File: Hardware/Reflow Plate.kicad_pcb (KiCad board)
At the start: 2 copper layers, 99.1 x 99.1 mm, 33 parts, among them J2 31-M-12, J3 Conn_02x03_Odd_Even, J4 Conn_02x03_Odd_Even, J5 Conn_02x03_Odd_Even, J6 Conn_02x03_Odd_Even, J7 Conn_01x04_Pin, Q2 Q_NMOS_GDS, U1 HUSB238, U2 AMS1117-3.3, U4 STM32F103RBTx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

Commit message: Add readme, bad power routing, final heater idea. Likely needs new layout.
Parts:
- removed U4: STM32F103RBTx, Package_QFP:LQFP-64_10x10mm_P0.5mm
- added G***: LOGO, footprints:Warning Hot, F.Cu at (139.7, 90.2)
- added J1: Barrel_Jack_MountingPin, footprints:DC Barrel, F.Cu at (97.4, 45.1)
- added MOSFET1: AONR21307, footprints:DFN8_3x3_EP_AOS, F.Cu at (113.5, 39.0)
- added U3: STM32F103CBTx, Package_QFP:LQFP-48_7x7mm_P0.5mm, F.Cu at (153.7, 42.5)
- J2: moved to B.Cu
- moved D2 73.3 mm to (114.2, 42.9)
- moved U1 63.3 mm to (105.4, 38.7)
- moved D1 61.1 mm to (104.1, 45.7), turned to -90 degrees
- moved R3 60.6 mm to (104.4, 36.4), turned to 180 degrees
- moved R2 59.4 mm to (109.9, 39.0), turned to 180 degrees
- moved R1 57.9 mm to (108.2, 37.7), turned to -90 degrees
- moved J2 34.7 mm to (105.4, 38.1), turned to 0 degrees
- moved U2 16.0 mm to (132.1, 25.4)
- moved J7 9.42 mm to (128.3, 38.7)
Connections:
- net GATE renamed Net-(U1-GATE)
- J3 pad 2: unconnected-(J3-Pin_2-Pad2) -> /Heater
- J3 pad 3: /Heater -> unconnected-(J3-Pin_3-Pad3)
- J3 pad 6: unconnected-(J3-Pin_6-Pad6) -> /Heater
- J5 pad 1: +24V -> Net-(J5-Pin_1)
- J5 pad 2: unconnected-(J5-Pin_2-Pad2) -> Net-(J5-Pin_1)
- J5 pad 3: +24V -> unconnected-(J5-Pin_3-Pad3)
- J5 pad 6: unconnected-(J5-Pin_6-Pad6) -> +24V
- Q2 pad 2: Net-(J6-Pin_1) -> Net-(J5-Pin_1)
- R1 pad 2: Net-(Q1-G) -> Net-(MOSFET1-G)
- R2 pad 1: Net-(Q1-G) -> Net-(J2-VBUS-PadA4)
- R2 pad 2: Net-(J2-VBUS-PadA4) -> Net-(MOSFET1-G)
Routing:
- net Net-(J2-VBUS-PadA4): track 0.00 -> 30.8 mm, vias 0 -> 3
- net +24V: track 0.00 -> 11.9 mm
- net UDB_D+: track 0.00 -> 10.8 mm, vias 0 -> 1
- net UDB_D-: track 0.00 -> 10.0 mm, vias 0 -> 1
- net Net-(D1-A): track 0.00 -> 6.86 mm
- net Net-(J2-CC2): track 0.00 -> 5.15 mm, vias 0 -> 1
- net Net-(J2-CC1): track 0.00 -> 4.88 mm, vias 0 -> 1
- net Net-(MOSFET1-G): track 0.00 -> 4.50 mm
- net /Heater: track 2943.6 -> 2941.4 mm
- net Net-(U1-GATE): track 0.00 -> 1.55 mm
- net Net-(U1-VIN): track 0.00 -> 1.31 mm

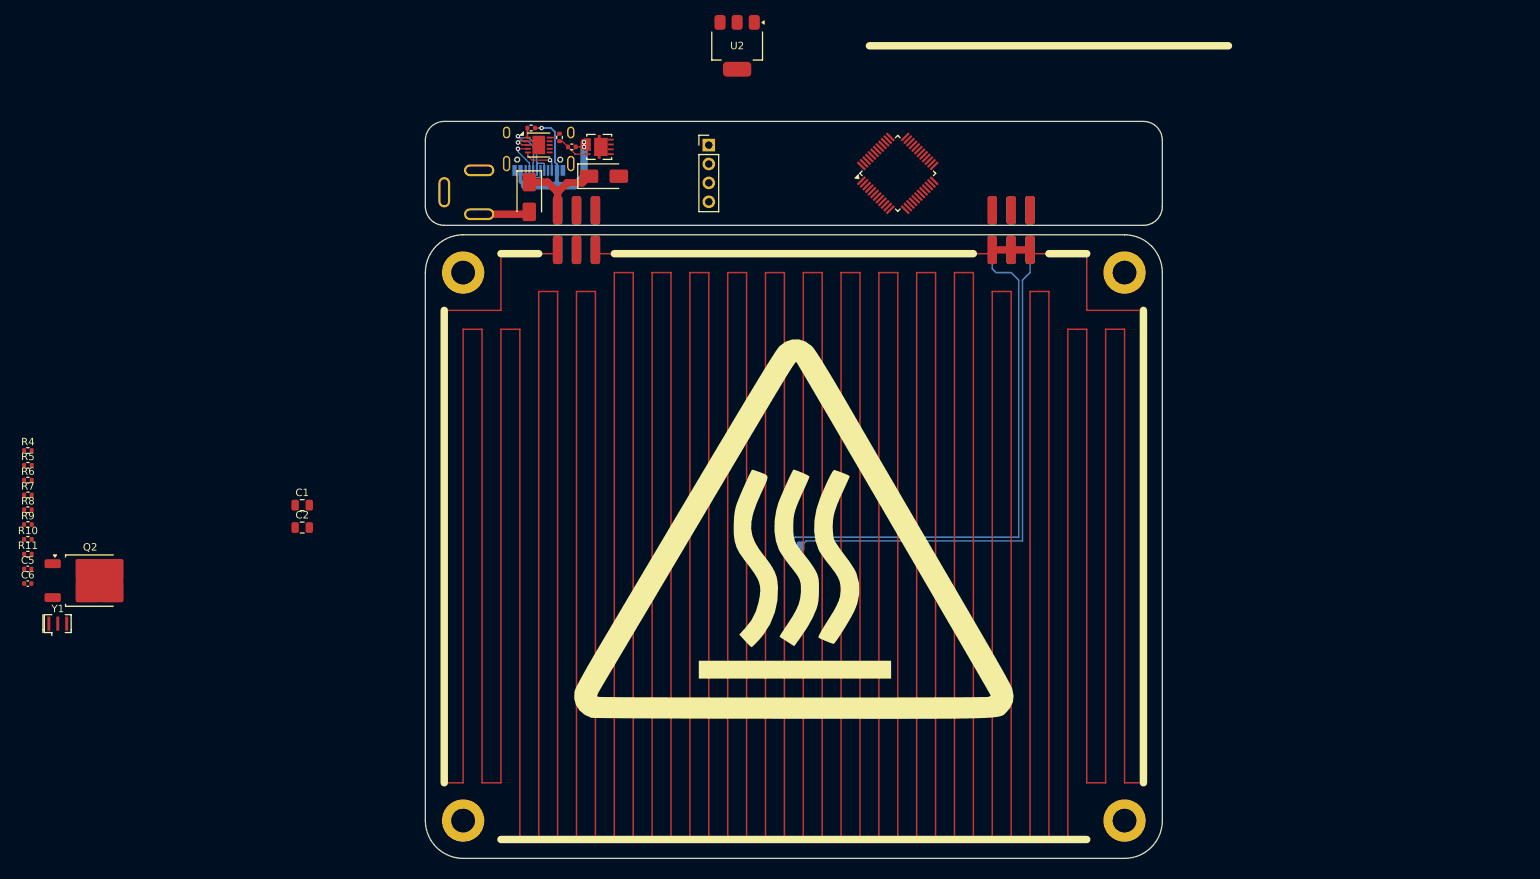
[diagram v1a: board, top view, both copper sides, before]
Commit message: Closer to final placement of power components. Shooting for single sided assembly. Still some scuffed placements. Really packed. Missing likely needed ground planes.
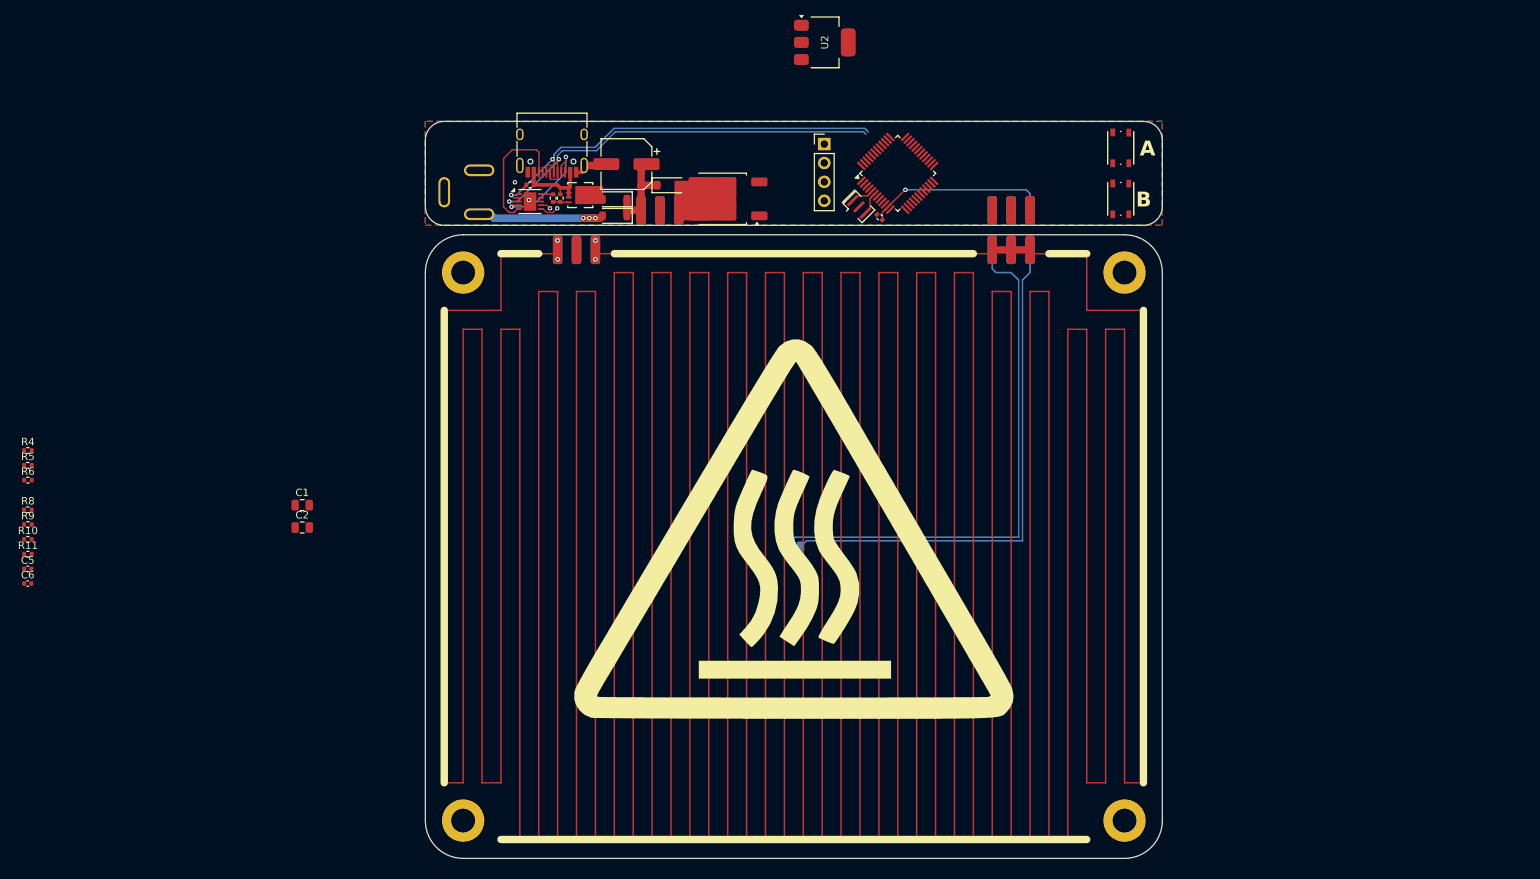
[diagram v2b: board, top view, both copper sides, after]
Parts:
- added C4: 220u, Capacitor_SMD:CP_Elec_6.3x7.7, F.Cu at (117.2, 41.3)
- added D3: D_Zener, Diode_SMD:D_SOD-123, F.Cu at (123.0, 44.1)
- added REF**: SW_Push_1P1T_NO_Vertical_Wuerth_434133025816, Button_Switch_SMD:SW_Push_1P1T_NO_Vertical_Wuerth_434133025816, F.Cu at (183.6, 39.1)
- added REF**: SW_Push_1P1T_NO_Vertical_Wuerth_434133025816, Button_Switch_SMD:SW_Push_1P1T_NO_Vertical_Wuerth_434133025816, F.Cu at (183.6, 46.0)
- D1, D2: footprint Diode_SMD:D_SMA -> Diode_SMD:D_SOD-123
- J2: moved to F.Cu
- moved Y1 121.4 mm to (148.5, 47.0), turned to -45 degrees
- moved R7 120.4 mm to (151.2, 48.4), turned to -45 degrees
- moved Q2 99.2 mm to (130.0, 46.0), turned to 180 degrees
- moved J7 33.2 mm to (161.3, 42.4)
- moved U2 11.8 mm to (143.9, 24.9), turned to 0 degrees
- moved D1 11.8 mm to (115.6, 48.3), turned to 180 degrees
- moved J5 11.2 mm to (121.7, 47.5)
- moved R1 8.20 mm to (107.3, 45.9)
- moved U1 7.68 mm to (104.2, 46.3)
- moved R3 7.65 mm to (104.2, 44.1)
- moved R2 7.06 mm to (108.3, 45.9), turned to -90 degrees
- moved MOSFET1 6.96 mm to (111.0, 45.5)
- moved D2 3.42 mm to (115.6, 46.0), turned to 180 degrees
- moved J2 1.80 mm to (107.2, 38.4), turned to 180 degrees
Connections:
- U3 pad 10: unconnected-(U3-PA0-Pad10) -> WKUP
- U3 pad 13: unconnected-(U3-PA3-Pad13) -> Heater_CTRL
- U3 pad 46: Heater_CTRL -> unconnected-(U3-PB9-Pad46)
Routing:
- net UDB_D-: track 10.0 -> 58.6 mm, vias 1 -> 2
- net UDB_D+: track 10.8 -> 58.1 mm, vias 1 -> 2
- net NTC_Measure: track 0.00 -> 24.6 mm, vias 0 -> 1
- net Net-(J2-VBUS-PadA4): track 30.8 -> 10.8 mm, vias 3 -> 0
- net Net-(J2-CC2): track 5.15 -> 17.2 mm, vias 1 -> 0
- net Net-(D1-A): track 6.86 -> 18.6 mm, vias 0 -> 3
- net Net-(J2-CC1): track 4.88 -> 14.8 mm, vias 1 -> 2
- net GND: track 0.00 -> 4.88 mm, vias 0 -> 2
- net Net-(U3-PD1): track 0.00 -> 3.10 mm
- net Net-(U3-PD0): track 0.00 -> 3.10 mm
- net SDA1: track 0.00 -> 2.62 mm, vias 0 -> 1
- net Net-(MOSFET1-G): track 4.50 -> 2.13 mm
- net SCL1: track 0.00 -> 1.40 mm, vias 0 -> 1
- net +24V: track 11.9 -> 12.8 mm
- net /Heater: vias 0 -> 4
- added copper zone on B.Cu, net GND
- added copper zone on F.Cu, net GND
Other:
- board text added: "A"
- board text added: "B"

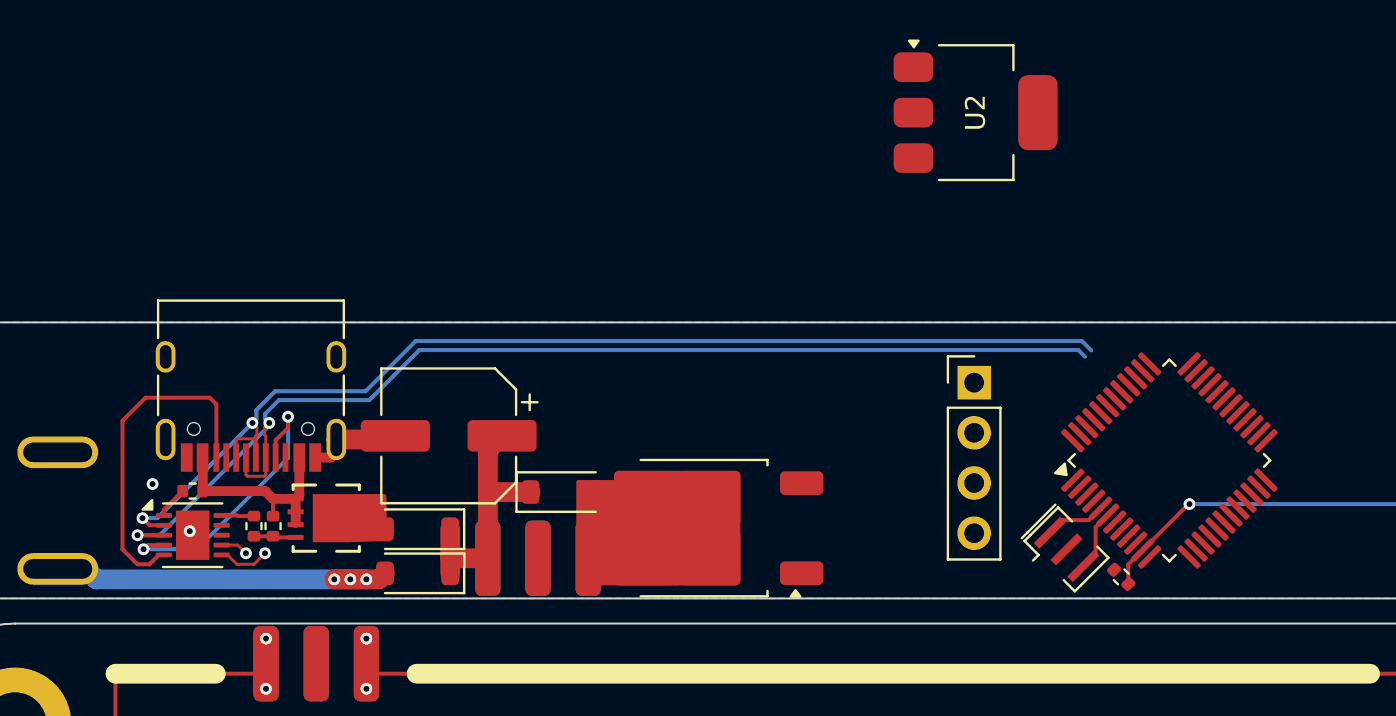
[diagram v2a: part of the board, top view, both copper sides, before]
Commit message: Final power layout. Changing LDO to SOT-23-5
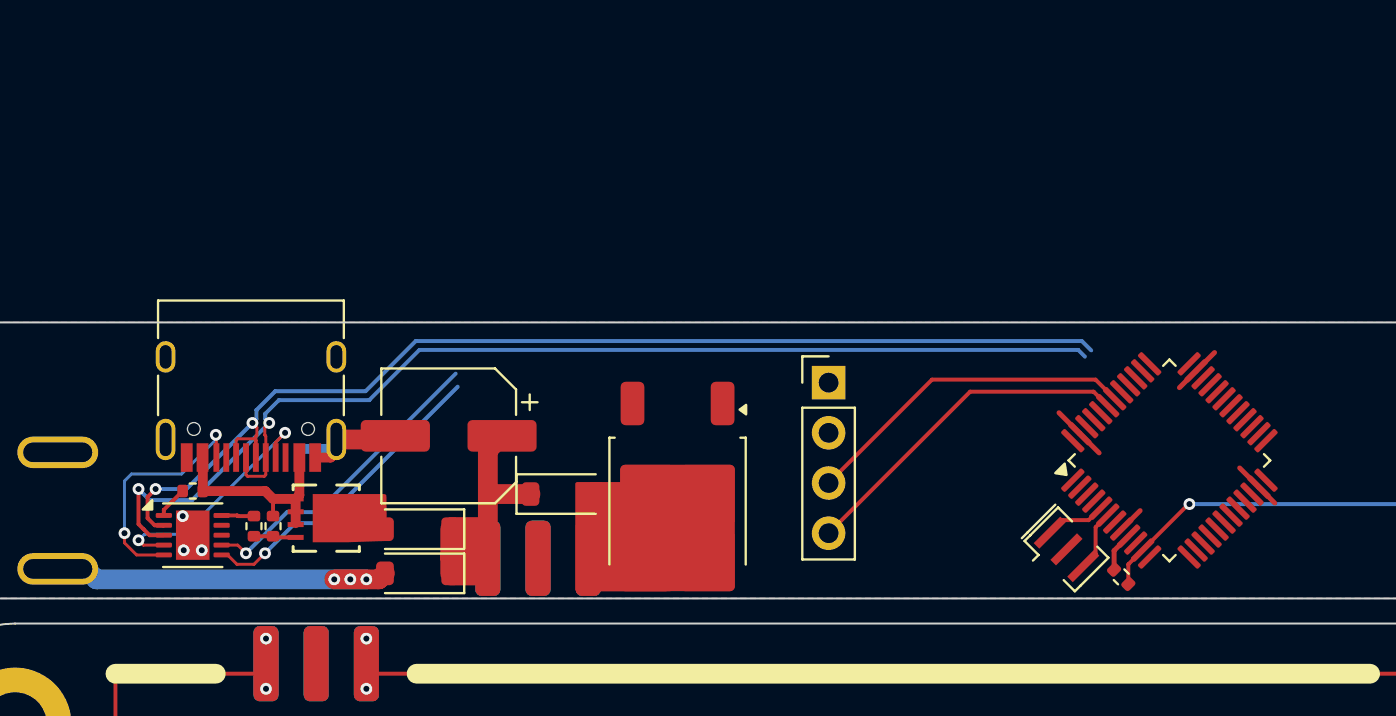
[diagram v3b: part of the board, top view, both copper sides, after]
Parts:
- removed U2: AMS1117-3.3, Package_TO_SOT_SMD:SOT-223-3_TabPin2
- moved J7 7.37 mm to (153.9, 42.4)
- moved Q2 1.78 mm to (128.8, 44.7), turned to -90 degrees
- moved D3 0.10 mm to (123.0, 44.2)
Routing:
- net SCL1: track 1.40 -> 32.8 mm
- net SDA1: track 2.62 -> 33.3 mm
- net GND: track 4.88 -> 16.1 mm, vias 2 -> 3
- net Net-(J2-CC2): track 17.2 -> 12.3 mm, vias 0 -> 2
- net Net-(J2-CC1): track 14.8 -> 12.5 mm
- net +3V3: track 0.00 -> 2.01 mm
- net UDB_D-: track 58.6 -> 60.1 mm
